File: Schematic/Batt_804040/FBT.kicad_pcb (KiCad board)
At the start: 2 copper layers, 41.9 x 72.7 mm, 17 parts, among them J1 TRRS Connector 3.5, J2 Conn_01x04, SW1 SW_SPDT

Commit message: Work on silkscreen logo
Made a mascot, "Mr. Tracker" which looks a lot like Mr. Lunt mixed with Pa Grape.
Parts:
- removed the J2 at (165.6, 104.9)
- added GY2: ~, My_Library:GY-271, B.Cu at (222.3, 111.8)
- added IMU2: ~, My_Library:GY-BMI160, F.Cu at (217.2, 111.8)
- added J2: TRRS Connector 3.5, My_Library:PJ-320A, F.Cu at (159.0, 117.7)
- added J2: TRRS Connector 3.5, My_Library:PJ-320A, F.Cu at (202.4, 120.4)
- moved GY2 18.4 mm to (169.9, 132.9)
- moved IMU2 18.4 mm to (169.9, 129.9)
- moved REF** 16.7 mm to (129.0, 120.6)
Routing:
- net ESP32_3V3: track 55.7 -> 87.8 mm
- net SDA_1: track 48.1 -> 69.2 mm, vias 2 -> 3
- net SCL_1: track 45.9 -> 62.6 mm, vias 2 -> 3
- net Net-(GY2-SDA): track 3.97 -> 17.1 mm, vias 0 -> 1
- net Net-(GY2-SCL): track 3.97 -> 13.7 mm
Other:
- board size 41.9 x 72.7 mm -> 99.1 x 89.6 mm

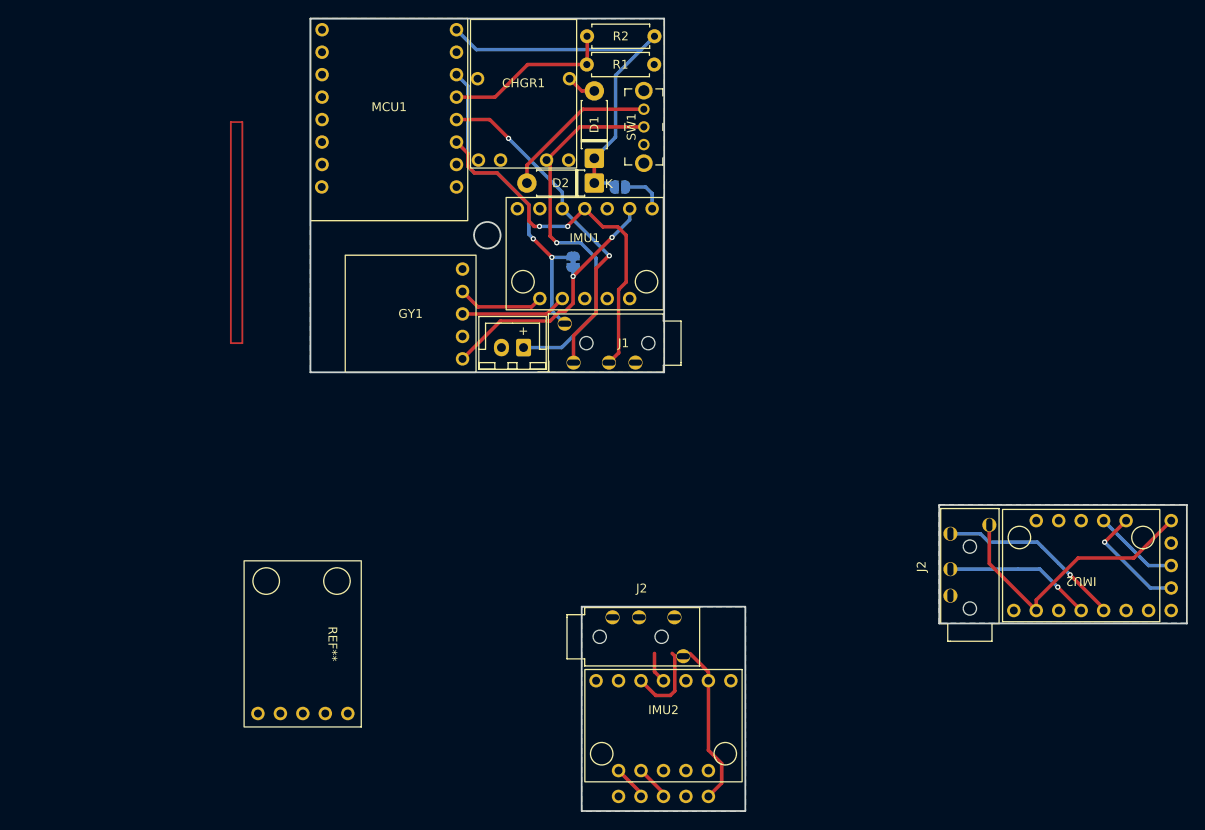
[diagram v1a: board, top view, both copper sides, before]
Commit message: Work on shell and PCB
Needed to do more work on the extended tracker
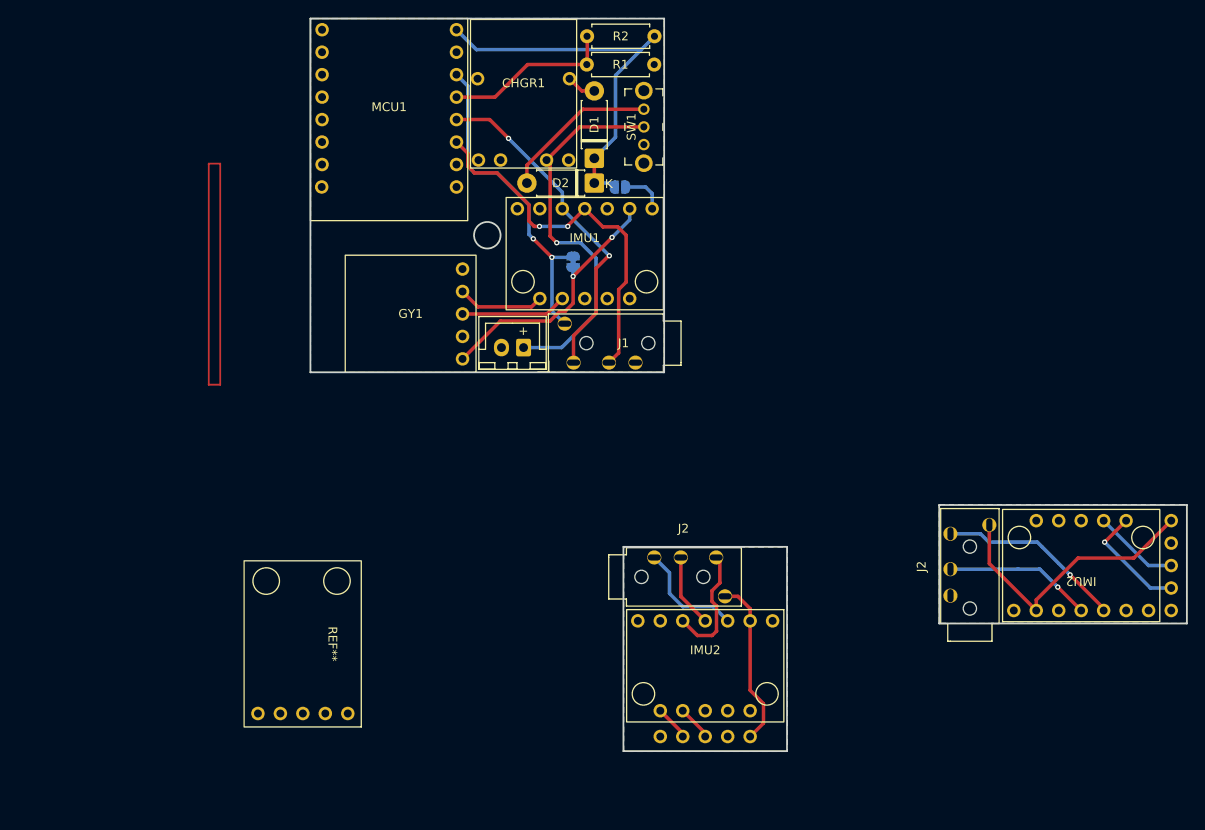
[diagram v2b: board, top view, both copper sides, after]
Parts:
- moved J2 8.25 mm to (163.7, 110.9)
- moved GY2 8.25 mm to (174.6, 126.2)
- moved IMU2 8.25 mm to (174.6, 123.2)
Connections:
- J2 pad R1: (no net) -> SDA_1
- J2 pad R2: (no net) -> SCL_1
- J2 pad S: (no net) -> GND
- J2 pad T: (no net) -> ESP32_3V3
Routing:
- net GND: track 0.00 -> 12.6 mm
- net SCL_1: track 62.6 -> 67.4 mm
- net SDA_1: track 69.2 -> 73.9 mm
- net ESP32_3V3: track 87.8 -> 88.6 mm
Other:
- board size 99.1 x 89.6 mm -> 99.1 x 82.8 mm

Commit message: work on PCBs, logos, and case
did more work on 18650 battery model
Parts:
- removed the GY2 at (222.3, 111.8)
- removed the IMU2 at (217.2, 111.8)
- removed the J2 at (163.7, 110.9)
- removed the J2 at (202.4, 120.4)
- added J2: TRRS Connector 3.5, My_Library:PJ-320A, F.Cu at (163.7, 111.0)
- moved REF** 20.4 mm to (149.3, 122.5)
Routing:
- net GND: track 12.6 -> 130.9 mm, vias 0 -> 2
- net ESP32_3V3: track 88.6 -> 59.7 mm, vias 2 -> 0
- net SDA_1: track 73.9 -> 57.2 mm, vias 3 -> 0
- net SCL_1: track 67.4 -> 53.6 mm, vias 3 -> 0
- net Net-(GY2-SDA): track 17.1 -> 3.97 mm, vias 1 -> 0
- net Net-(GY1-VIN): track 29.2 -> 39.6 mm
- net Net-(GY2-SCL): track 13.7 -> 3.97 mm
- net ESP32_5V5: track 43.7 -> 47.9 mm, vias 0 -> 1
- net +BATT: track 43.6 -> 44.1 mm, vias 1 -> 0
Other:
- board size 99.1 x 82.8 mm -> 53.9 x 82.8 mm
- board text added: "Type A Rev. 1.0"
- board text added: "Type B Rev. 1.0"
- board text added: "www.github.com"

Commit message: Final touches for fabrication
Sent designs off to JLBPCB... hopefully they work...
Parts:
- added REF**: MountingHole_3mm, MountingHole:MountingHole_3mm, B.Cu at (150.0, 74.5)
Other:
- outline, holes or cut-outs redrawn
- board text added: "BATT"
- board text added: "JLCJLCJLCJLC"
- board text added: "UFBTM Type B Rev. 1.0"
- board text added: "github.com/DrGlaucous/UFBTM"
- board text removed: "Type B Rev. 1.0"
- board text removed: "www.github.com"

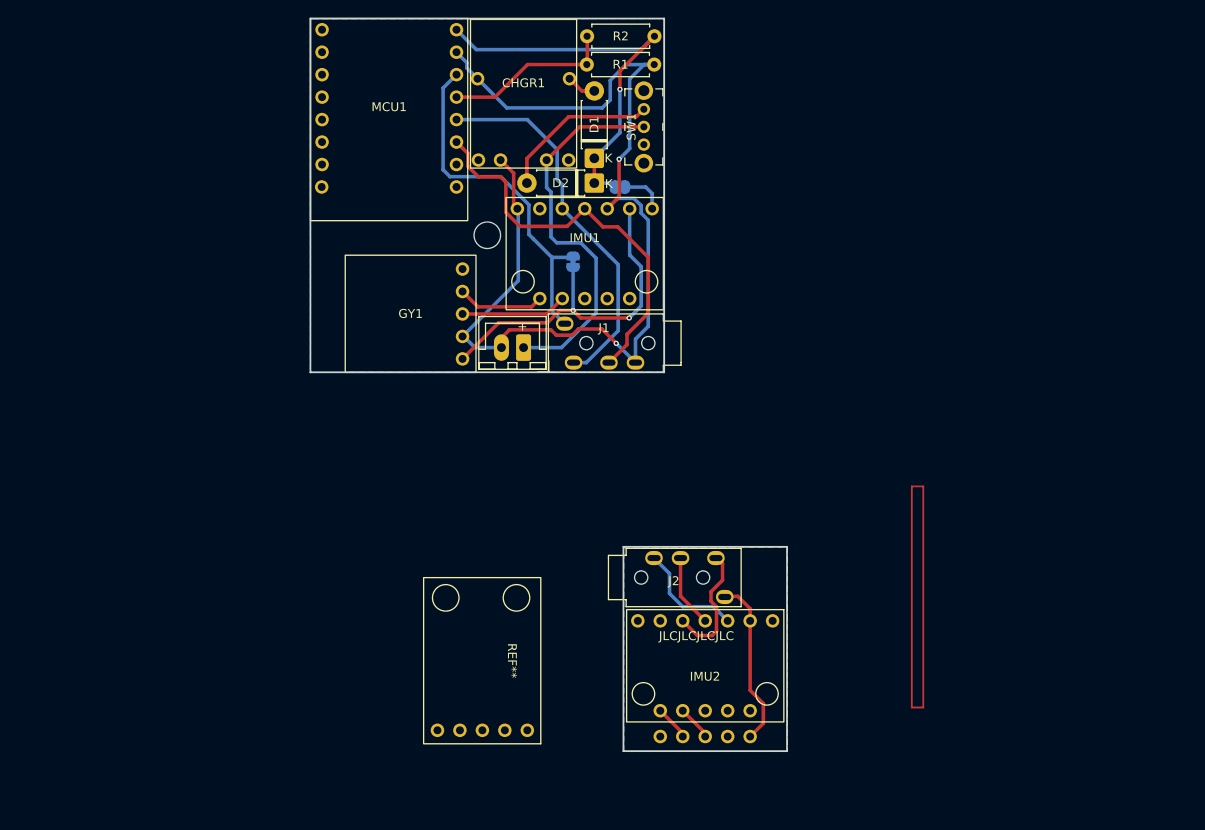
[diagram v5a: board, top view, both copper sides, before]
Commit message: Rework MrTracker footprint to support the big lx-lbes
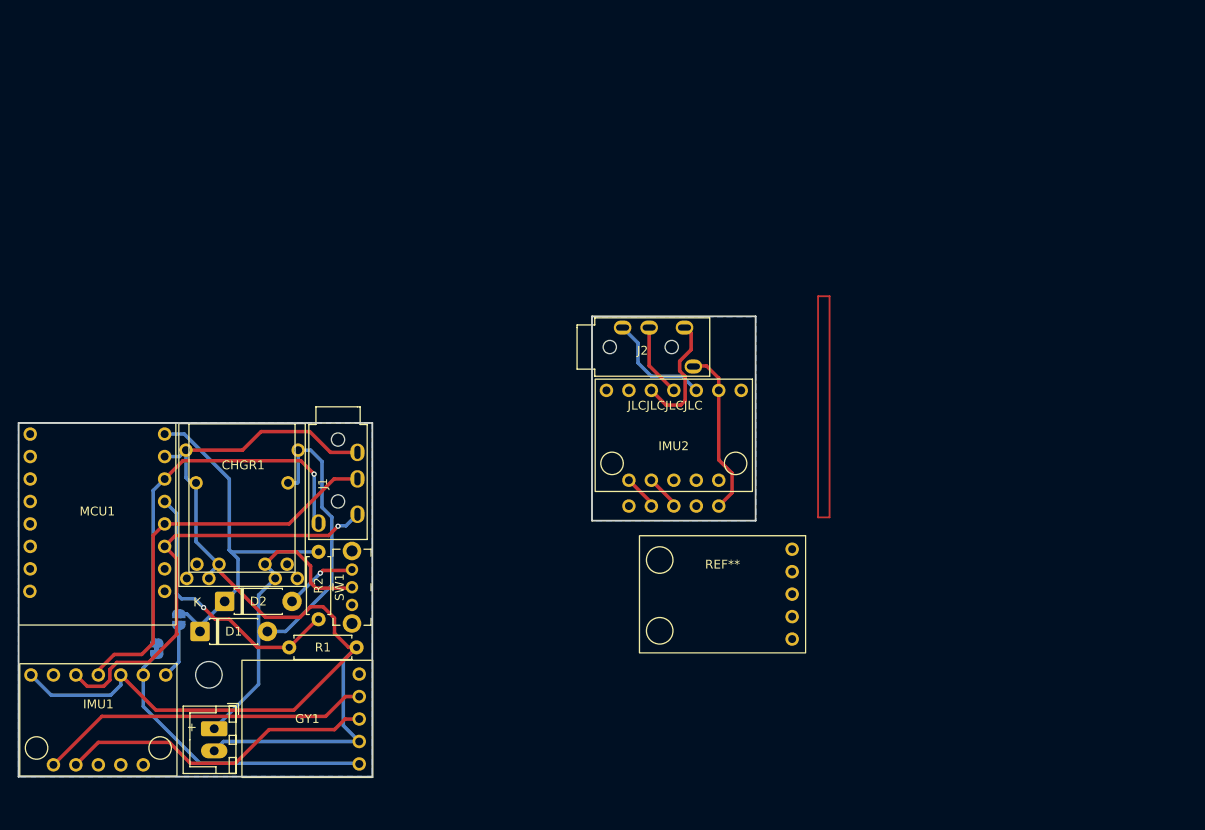
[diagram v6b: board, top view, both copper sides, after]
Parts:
- added CHGR2: ~, My_Library:LX-LBES-Big, F.Cu at (129.4, 114.2)
- moved IMU1 76.2 mm to (106.0, 129.3)
- moved R1 74.0 mm to (135.2, 121.1)
- moved R2 72.6 mm to (130.9, 117.9), turned to 90 degrees
- moved JP1 69.9 mm to (115.1, 118.0), turned to 90 degrees
- moved D1 69.6 mm to (117.5, 119.3), turned to 0 degrees
- moved JP2 64.3 mm to (112.6, 121.2)
- moved D2 63.1 mm to (120.3, 115.9), turned to 0 degrees
- moved SW1 61.6 mm to (134.7, 114.3)
- moved REF** 58.8 mm to (118.5, 124.2)
- moved MCU1 56.4 mm to (105.9, 107.1)
- moved CHGR1 55.7 mm to (128.3, 112.6)
- moved BT1 55.5 mm to (119.1, 130.3), turned to -90 degrees
- moved GY1 47.3 mm to (130.5, 129.2)
- moved J1 36.9 mm to (135.3, 93.9), turned to -90 degrees
- moved REF** 28.2 mm to (176.5, 115.2), turned to 0 degrees
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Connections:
- net Net-(CHGR1-5_VIN) renamed /5_VIN_LX
- MCU1 pad 11: SCL_1 -> SDA_1
- MCU1 pad 12: SDA_1 -> SCL_1
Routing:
- net /5_VIN_LX: track 3.37 -> 32.5 mm
- net Net-(GY1-SDA): track 9.85 -> 37.8 mm
- net Net-(GY1-SCL): track 12.0 -> 36.1 mm
- net GND: track 130.8 -> 148.1 mm, vias 2 -> 0
- net BATTERY_READER: track 19.5 -> 30.9 mm, vias 0 -> 1
- net Net-(D2-A): track 18.3 -> 8.15 mm, vias 0 -> 1
- net +BATT: track 44.1 -> 35.1 mm
- net Net-(GY1-VIN): track 39.6 -> 33.6 mm, vias 2 -> 0
- net SDA_1: track 57.3 -> 63.1 mm, vias 0 -> 1
- net ESP32_5V5: track 47.9 -> 42.5 mm, vias 1 -> 0
- net ESP32_3V3: track 59.7 -> 62.5 mm, vias 0 -> 1
- net Net-(IMU1-VIN): track 5.16 -> 6.23 mm
- net SCL_1: track 53.6 -> 54.2 mm
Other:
- board size 53.9 x 82.8 mm -> 83.3 x 52 mm
- board text added: "Type A Rev. 2.0"
- board text removed: "Type A Rev. 1.0"
